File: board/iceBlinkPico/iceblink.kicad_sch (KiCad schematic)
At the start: 54 parts, among them J1 USB4105-GF-A, J2 Left, J3 Right, U1 W25Q128JV, U2 MIC5365-1-2YD5, U3 MIC5318-3-3YD5, U4 ICE40UP5K-SG48ITR, X1 IQXO-791

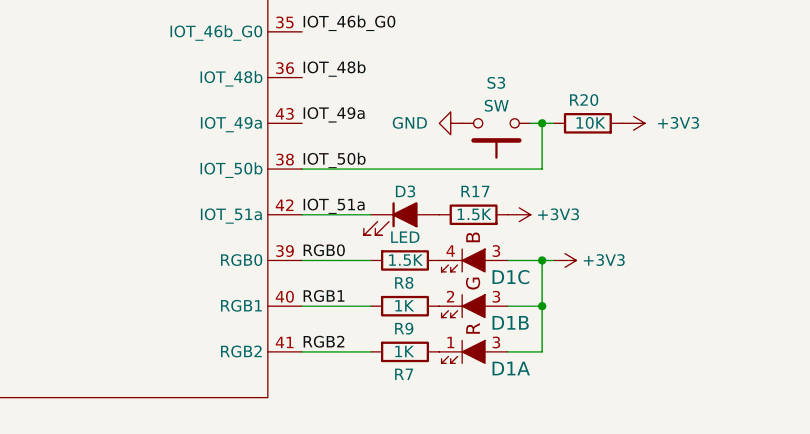
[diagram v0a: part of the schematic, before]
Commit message: Update to PCB to fix LED current limiting resistor values.
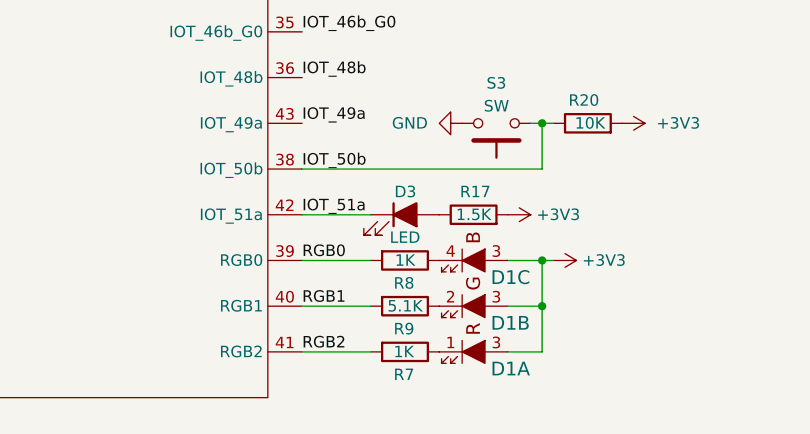
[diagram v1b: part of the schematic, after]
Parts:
- R8: value 1.5K -> 1K
- R9: value 1K -> 5.1K
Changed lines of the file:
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@@
 	(label "IOT_41a"
 		(at 182.88 125.73 0)
-		(fields_autoplaced yes)
 		(effects
 			(font
@@
 	(label "IOB_29b"
 		(at 182.88 95.25 0)
-		(fields_autoplaced yes)
 		(effects
 			(font
@@
 	(label "IOB_2a"
 		(at 182.88 44.45 0)
-		(fields_autoplaced yes)
 		(effects
 			(font
@@
 	(label "IOT_51a"
 		(at 182.88 171.45 0)
-		(fields_autoplaced yes)
 		(effects
 			(font
@@
 	(label "IOT_46b_G0"
 		(at 182.88 151.13 0)
-		(fields_autoplaced yes)
 		(effects
 			(font
@@
 	(label "IOB_9b"
 		(at 292.1 124.46 180)
-		(fields_autoplaced yes)
 		(effects
 			(font
@@
 	(label "IOB_5a"
 		(at 292.1 139.7 180)
-		(fields_autoplaced yes)
 		(effects
 			(font
@@
 	(label "IOT_49a"
 		(at 292.1 144.78 180)
-		(fields_autoplaced yes)
 		(effects
 			(font
@@
 	(label "IOB_9b"
 		(at 182.88 74.93 0)
-		(fields_autoplaced yes)
 		(effects
 			(font
@@
 	(label "IOB_31b"
 		(at 254 111.76 0)
-		(fields_autoplaced yes)
 		(effects
 			(font
@@
 	(label "IOB_20a"
 		(at 292.1 111.76 180)
-		(fields_autoplaced yes)
 		(effects
 			(font
@@
 	(label "IOT_50b"
 		(at 182.88 166.37 0)
-		(fields_autoplaced yes)
 		(effects
 			(font
@@
 	(label "IOB_0a"
 		(at 182.88 39.37 0)
-		(fields_autoplaced yes)
 		(effects
 			(font
@@
 	(label "IOT_44b"
 		(at 254 139.7 0)
-		(fields_autoplaced yes)
 		(effects
 			(font
@@
 	(label "IOT_37a"
 		(at 182.88 110.49 0)
-		(fields_autoplaced yes)
 		(effects
 			(font
@@
 	(label "IOB_2a"
 		(at 292.1 132.08 180)
-		(fields_autoplaced yes)
 		(effects
 			(font
@@
 	(label "IOT_42b"
 		(at 254 132.08 0)
-		(fields_autoplaced yes)
 		(effects
 			(font
@@
 	(label "IOT_39a"
 		(at 182.88 120.65 0)
-		(fields_autoplaced yes)
 		(effects
 			(font
@@
 	(label "IOT_43a"
 		(at 254 137.16 0)
-		(fields_autoplaced yes)
 		(effects
 			(font
@@
 	(label "IOT_41a"
 		(at 254 129.54 0)
-		(fields_autoplaced yes)
 		(effects
 			(font
@@
 	(label "IOT_45a_G1"
 		(at 182.88 146.05 0)
-		(fields_autoplaced yes)
 		(effects
 			(font
@@
 	(label "IOB_3b_G6"
 		(at 182.88 49.53 0)
-		(fields_autoplaced yes)
 		(effects
 			(font
@@
 	(label "RGB1"
 		(at 254 149.86 0)
-		(fields_autoplaced yes)
 		(effects
 			(font
@@
 	(label "IOB_31b"
 		(at 182.88 100.33 0)
-		(fields_autoplaced yes)
 		(effects
 			(font
@@
 	(label "IOB_5a"
 		(at 182.88 59.69 0)
-		(fields_autoplaced yes)
 		(effects
 			(font
@@
 	(label "IOB_4a"
 		(at 292.1 129.54 180)
-		(fields_autoplaced yes)
 		(effects
 			(font
@@
 	(label "IOT_38b"
 		(at 182.88 115.57 0)
-		(fields_autoplaced yes)
 		(effects
 			(font
@@
 	(label "IOT_36b"
 		(at 182.88 105.41 0)
-		(fields_autoplaced yes)
 		(effects
 			(font
@@
 	(label "IOB_8a"
 		(at 182.88 69.85 0)
-		(fields_autoplaced yes)
 		(effects
 			(font
@@
 	(label "IOB_20a"
 		(at 182.88 90.17 0)
-		(fields_autoplaced yes)
 		(effects
 			(font
@@
 	(label "RGB2"
 		(at 254 152.4 0)
-		(fields_autoplaced yes)
 		(effects
 			(font
@@
 	(label "IOB_6a"
 		(at 292.1 127 180)
-		(fields_autoplaced yes)
 		(effects
 			(font
@@
 	(label "IOT_42b"
 		(at 182.88 130.81 0)
-		(fields_autoplaced yes)
 		(effects
 			(font
@@
 	(label "IOB_8a"
 		(at 292.1 119.38 180)
-		(fields_autoplaced yes)
 		(effects
 			(font
@@
 	(label "IOT_39a"
 		(at 254 124.46 0)
-		(fields_autoplaced yes)
 		(effects
 			(font
@@
 	(label "IOT_38b"
 		(at 254 127 0)
-		(fields_autoplaced yes)
 		(effects
 			(font
@@
 	(label "IOB_13b"
 		(at 182.88 80.01 0)
-		(fields_autoplaced yes)
 		(effects
 			(font
@@
 	(label "IOT_37a"
 		(at 254 116.84 0)
-		(fields_autoplaced yes)
 		(effects
 			(font
@@
 	(label "IOB_13b"
 		(at 292.1 116.84 180)
-		(fields_autoplaced yes)
 		(effects
 			(font
@@
 	(label "IOB_4a"
 		(at 182.88 54.61 0)
-		(fields_autoplaced yes)
 		(effects
 			(font
@@
 	(label "RGB0"
 		(at 182.88 176.53 0)
-		(fields_autoplaced yes)
 		(effects
 			(font
@@
 	(label "IOT_45a_G1"
 		(at 292.1 149.86 180)
-		(fields_autoplaced yes)
 		(effects
 			(font
@@
 	(label "IOB_3b_G6"
 		(at 292.1 142.24 180)
-		(fields_autoplaced yes)
 		(effects
 			(font
@@
 	(label "IOT_36b"
 		(at 254 119.38 0)
-		(fields_autoplaced yes)
 		(effects
 			(font
@@
 	(label "IOB_18a"
 		(at 182.88 85.09 0)
-		(fields_autoplaced yes)
 		(effects
 			(font
@@
 	(label "RGB2"
 		(at 182.88 186.69 0)
-		(fields_autoplaced yes)
 		(effects
 			(font
@@
 	(label "IOT_49a"
 		(at 182.88 161.29 0)
-		(fields_autoplaced yes)
 		(effects
 			(font
@@
 	(label "IOB_18a"
 		(at 292.1 114.3 180)
-		(fields_autoplaced yes)
 		(effects
 			(font
@@
 	(label "IOT_48b"
 		(at 182.88 156.21 0)
-		(fields_autoplaced yes)
 		(effects
 			(font
@@
 	(label "IOT_44b"
 		(at 182.88 140.97 0)
-		(fields_autoplaced yes)
 		(effects
 			(font
@@
 	(label "IOT_48b"
 		(at 292.1 152.4 180)
-		(fields_autoplaced yes)
 		(effects
 			(font
@@
 	(label "RGB0"
 		(at 254 144.78 0)
-		(fields_autoplaced yes)
 		(effects
 			(font
@@
 	(label "IOT_43a"
 		(at 182.88 135.89 0)
-		(fields_autoplaced yes)
 		(effects
 			(font
@@
 	(label "IOT_46b_G0"
 		(at 254 142.24 0)
-		(fields_autoplaced yes)
 		(effects
 			(font
@@
 	(label "IOB_0a"
 		(at 292.1 137.16 180)
-		(fields_autoplaced yes)
 		(effects
 			(font
@@
 	(label "IOB_6a"
 		(at 182.88 64.77 0)
-		(fields_autoplaced yes)
 		(effects
 			(font
@@
 	(label "RGB1"
 		(at 182.88 181.61 0)
-		(fields_autoplaced yes)
 		(effects
 			(font
@@
 	(label "IOB_29b"
 		(at 254 114.3 0)
-		(fields_autoplaced yes)
 		(effects
 			(font
@@
 			)
 		)
-		(property "Value" "1K"
-			(at 193.04 181.61 90)
+		(property "Value" "5.1K"
+			(at 194.31 181.61 90)
 			(effects
 				(font
 					(size 1.27 1.27)
 				)
-				(justify left)
 			)
 		)
@@
 			)
 		)
-		(property "Value" "1.5K"
+		(property "Value" "1K"
 			(at 194.31 176.53 90)
 			(effects
